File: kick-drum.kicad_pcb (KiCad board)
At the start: 2 copper layers, 30 x 232.4 mm, 69 parts, among them J1 Conn_02x05_Odd_Even, J2 GATE, J3 ACCENT CV, J4 PITCH CV, J5 OUTPUT, Q1 BCM857DS,135, Q2 BC547C, Q3 BCM847DS,135, U1 TL074

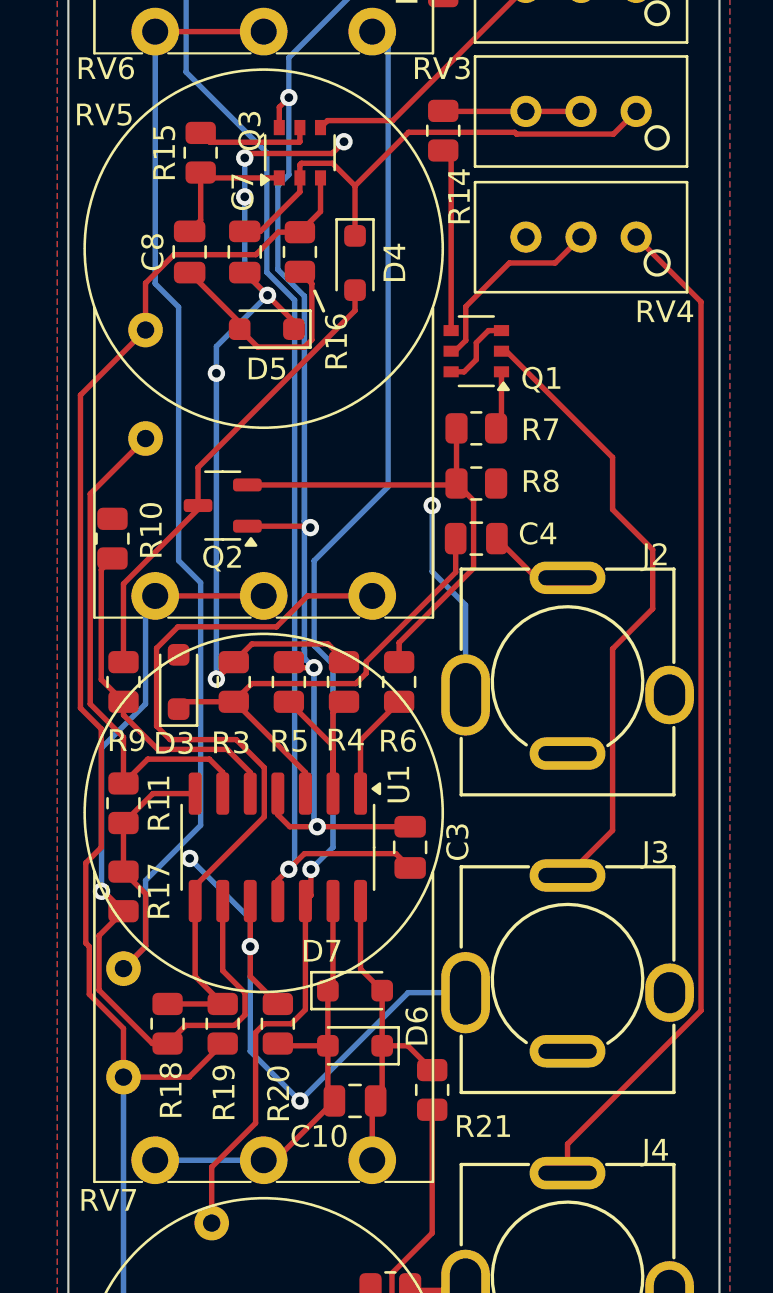
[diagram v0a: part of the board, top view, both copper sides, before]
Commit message: update PCB for input protection
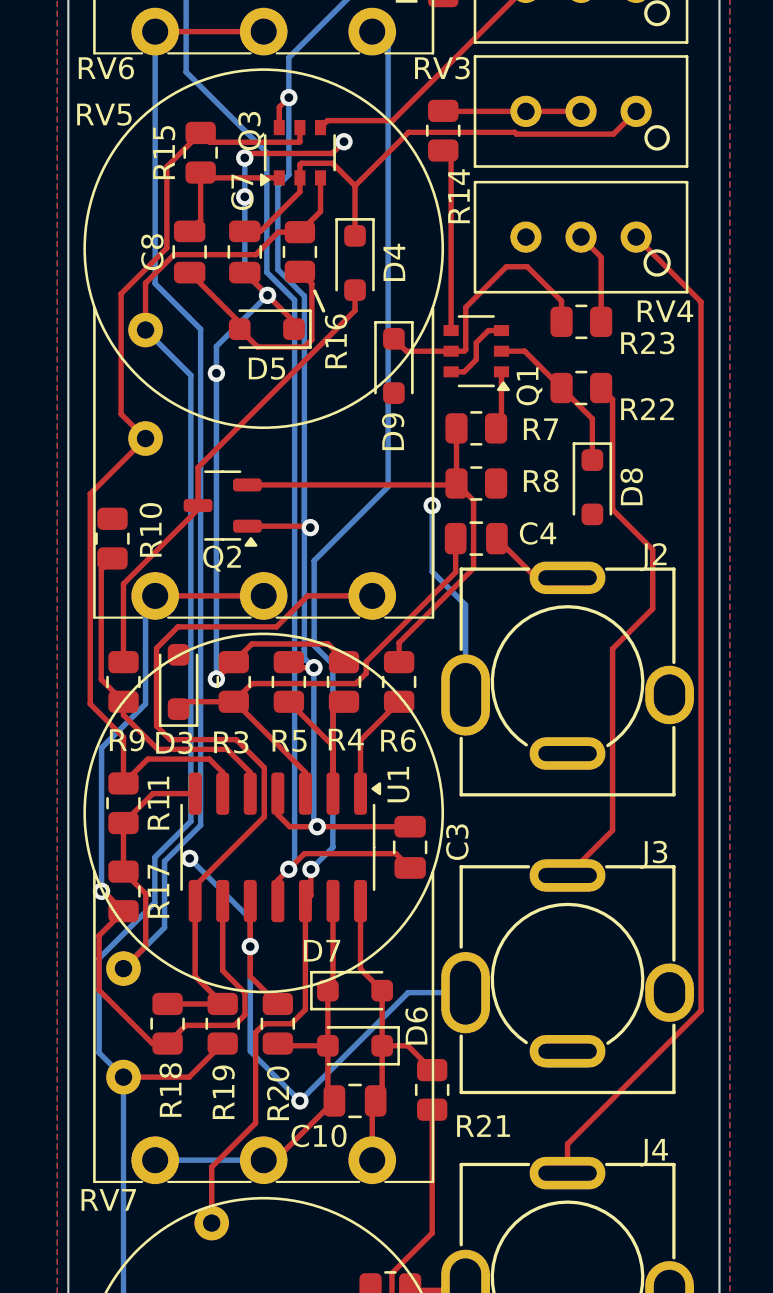
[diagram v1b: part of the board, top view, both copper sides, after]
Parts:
- added D8: 1N4148, Diode_SMD:D_SOD-323_HandSoldering, F.Cu at (110.7, 42.7)
- added D9: 1N4148, Diode_SMD:D_SOD-323_HandSoldering, F.Cu at (101.6, 37.1)
- added R22: 10K, Resistor_SMD:R_0805_2012Metric, F.Cu at (110.2, 38.1)
- added R23: 10K, Resistor_SMD:R_0805_2012Metric, F.Cu at (110.2, 35.1)
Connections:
- C5 pad 1: Net-(U1B--) -> Net-(Q3B-B2)
- Q1 pad 2: /ACCENT_CV -> Net-(D8-K)
- Q1 pad 5: Net-(Q1B-B2) -> Net-(D9-K)
- R11 pad 1: Net-(U1B--) -> Net-(Q3B-B2)
- RV4 pad 2: Net-(Q1B-B2) -> Net-(R23-Pad2)
- U1 pad 6: Net-(U1B--) -> Net-(Q3B-B2)
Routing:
- net Net-(Q3B-B2): track 5.41 -> 45.3 mm
- net Net-(U1B--): track 23.8 -> 0.00 mm
- net Net-(D9-K): track 0.00 -> 12.3 mm
- net Net-(Q1B-B2): track 8.90 -> 0.00 mm
- net Net-(D8-K): track 0.00 -> 7.38 mm
- net Net-(R23-Pad2): track 0.00 -> 4.29 mm
- net /ACCENT_CV: track 28.6 -> 25.1 mm
- net Net-(D6-A): track 20.3 -> 19.7 mm

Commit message: v1 ready
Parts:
- Q2: value BC547C -> BC847; footprint Package_TO_SOT_SMD:SOT-23-3 -> Package_TO_SOT_SMD:SOT-23
- moved Q2 2.29 mm to (95.9, 42.8), turned to -90 degrees
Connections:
- C5 pad 1: Net-(Q3B-B2) -> Net-(U1B--)
- Q2 pad 1: +12V -> Net-(Q2-B)
- Q2 pad 2: Net-(Q2-B) -> Net-(D4-A)
- Q2 pad 3: Net-(D4-A) -> +12V
- R11 pad 1: Net-(Q3B-B2) -> Net-(U1B--)
- U1 pad 6: Net-(Q3B-B2) -> Net-(U1B--)
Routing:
- net Net-(Q3B-B2): track 45.3 -> 5.41 mm
- net Net-(U1B--): track 0.00 -> 23.8 mm
- net Net-(Q2-B): track 22.1 -> 20.4 mm
- net Net-(D4-A): track 21.4 -> 23.0 mm
- net +12V: track 77.8 -> 77.0 mm
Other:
- board text added: "thismatters/kick-drum/v1"
- board text removed: "thismatters/kick-drum/v0"
